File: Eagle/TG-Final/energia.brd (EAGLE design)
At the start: 172.7 x 172.7 mm, 55 parts, among them IC1 7812T, IC2 7805, IC3 AZ1117, IC4 7806T, Q1 TIP2955, T1 2N3904

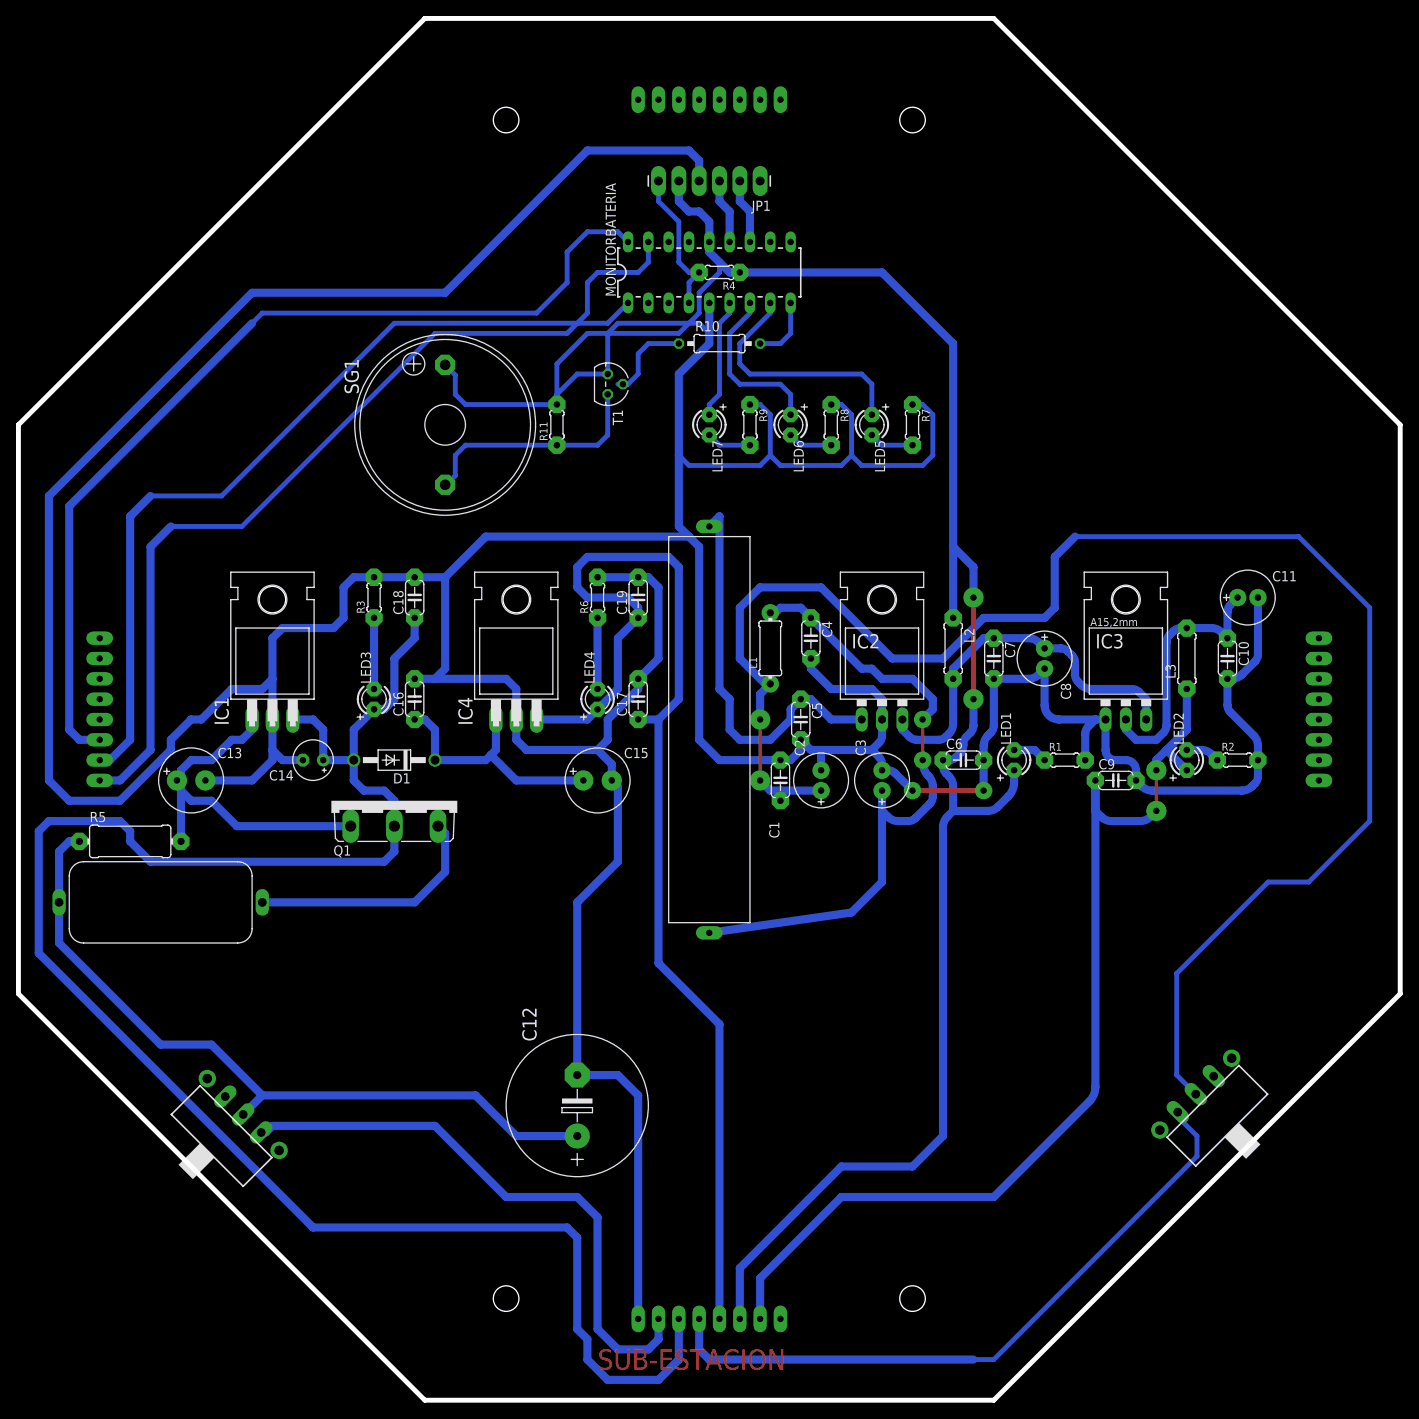
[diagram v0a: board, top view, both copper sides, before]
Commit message: Placa Sub-Estación. Lista
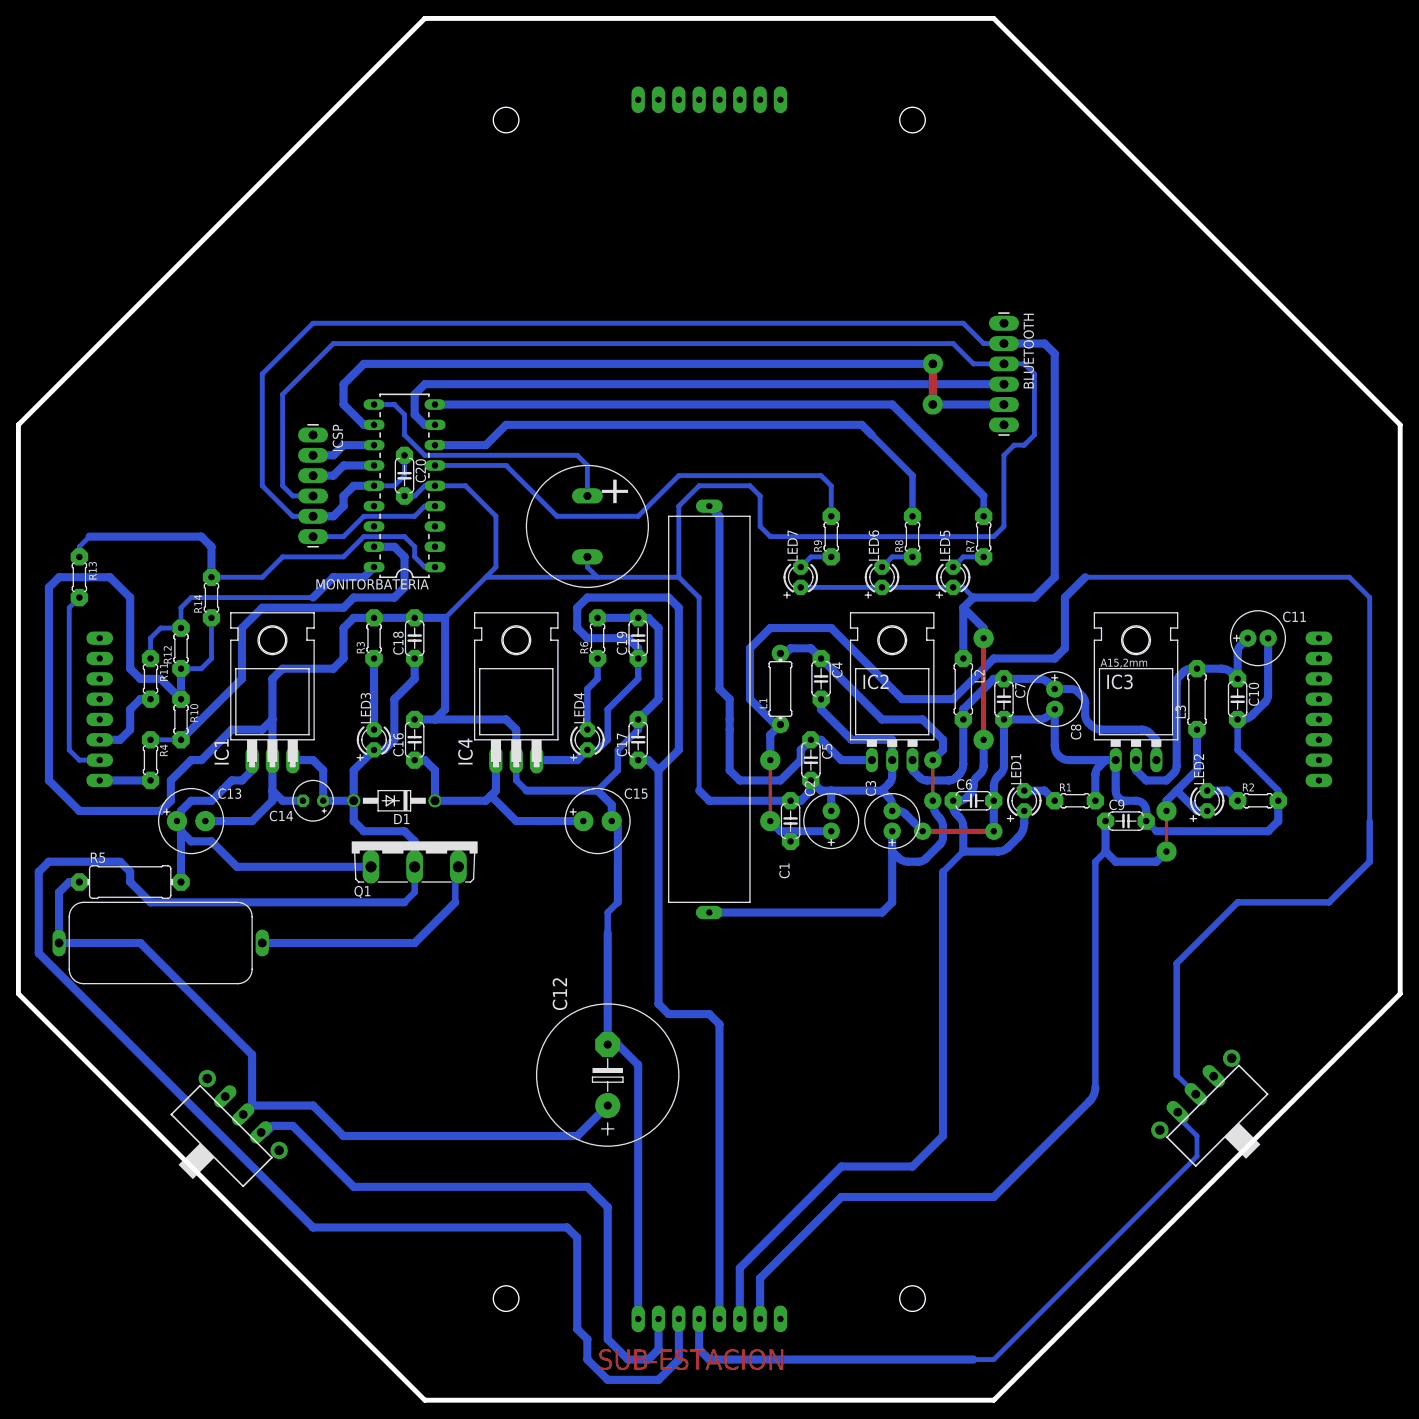
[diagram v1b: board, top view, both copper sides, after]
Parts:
- removed JP1: (no value), SparkFun:1X06_LONGPADS
- removed SG1: EB2209A, buzzer:EB2209A
- removed T1: 2N3904, transistor:TO92
- added BLUETOOTH, ICSP: (no value), SparkFun:1X06_LONGPADS
- added C20: 0.1uf, rcl:C050-024X044
- added R12, R14: 15K, rcl:0204/5
- added R13: 20K, rcl:0204/5
- added U$10: BUZZER, aasanchez:BUZZER
- LED5, LED6, LED7: value (none) -> RED
- R10: value 4K7 -> 15K; device rcl:0207/10 -> rcl:0204/5
- R11: value 4K7 -> 20K
- R4: value 1k -> 20K
- moved R4 93.7 mm to (-34.3, 80.0), turned to 270 degrees
- moved R10 82.1 mm to (-30.5, 85.1), turned to 270 degrees
- moved R11 59.9 mm to (-34.3, 90.2), turned to 270 degrees
- moved MONITORBATERIA 46.5 mm to (-2.54, 114.3), turned to 90 degrees
- moved LED6 22.2 mm to (57.1, 102.9), turned to 90 degrees
- moved LED7 22.2 mm to (47.0, 102.9), turned to 90 degrees
- moved LED5 21.6 mm to (66.0, 102.9), turned to 90 degrees
- moved R8 17.3 mm to (61.0, 108.0), turned to 90 degrees
- moved R9 17.3 mm to (50.8, 108.0), turned to 90 degrees
- moved R7 16.6 mm to (69.8, 108.0), turned to 90 degrees
- moved Q1 5.68 mm to (-1.27, 69.8)
- moved LED2 5.68 mm to (97.8, 74.9)
- moved R2 5.68 mm to (104.1, 74.9)
- moved C12 5.39 mm to (22.9, 40.6)
- moved IC3 5.24 mm to (88.9, 83.8)
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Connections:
- removed net N$23: MONITORBATERIA.9, R10.2
- removed net N$25: R11.1, SG1.-, T1.1
- new net AN0: MONITORBATERIA.17, R10.2, R4.1
- new net AN1: MONITORBATERIA.18, R11.1, R12.2
- new net AN2: MONITORBATERIA.1, R13.1, R14.2
- new net RX: BLUETOOTH.4, MONITORBATERIA.8
- new net TX: BLUETOOTH.5, MONITORBATERIA.11
- net N$15: now also R7.1; no longer R7.2
- net N$16: now also LED7.K, R9.1; no longer LED6.K, R8.2
- net N$19: now also LED6.K, R8.1; no longer LED7.K, R9.2
- net N$2: now also ICSP.6; no longer JP1.6, R4.2
- net N$20: now also R9.2; no longer LED7.A
- net N$21: now also R8.2; no longer LED6.A
- net N$22: now also MONITORBATERIA.9, R7.2; no longer LED5.A, MONITORBATERIA.8
- net N$24: now also MONITORBATERIA.10, U$10.+; no longer R10.1, T1.2
- net N$5: now also ICSP.3; no longer JP1.3
- net N$6: now also ICSP.2; no longer JP1.2
- net SENSE1: now also R4.2; no longer MONITORBATERIA.17
- net SENSE2: now also R11.2; no longer MONITORBATERIA.18
- net SENSE3: now also R13.2; no longer MONITORBATERIA.1
- net VDD: now also BLUETOOTH.2, C20.1, ICSP.5, LED5.A, LED6.A, LED7.A; no longer JP1.5, R11.2, R4.1, SG1.+
- net VSS: now also BLUETOOTH.3, C20.2, ICSP.4, R10.1, R12.1, R14.1, U$10.-; no longer JP1.4, R7.1, R8.1, R9.1, T1.3
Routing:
- net SENSE2: track 119.1 -> 9.94 mm
- net SENSE1: track 115.1 -> 6.35 mm
- net TX: track 0.00 -> 96.1 mm, vias 0 -> 2
- net SENSE3: track 106.1 -> 23.9 mm
- net RX: track 0.00 -> 79.8 mm
- net VDD: track 266.7 -> 331.4 mm
- net AN2: track 0.00 -> 55.0 mm
- net AN0: track 0.00 -> 51.5 mm
- net N$21: track 21.2 -> 68.5 mm
- net N$22: track 30.6 -> 75.9 mm
- net N$20: track 15.0 -> 58.6 mm
- net AN1: track 0.00 -> 35.7 mm
- net N$25: track 29.5 -> 0.00 mm
- net VSS: track 707.5 -> 734.9 mm
- net N$24: track 11.2 -> 35.1 mm
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
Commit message: Placa de Control Motores y Comunicación
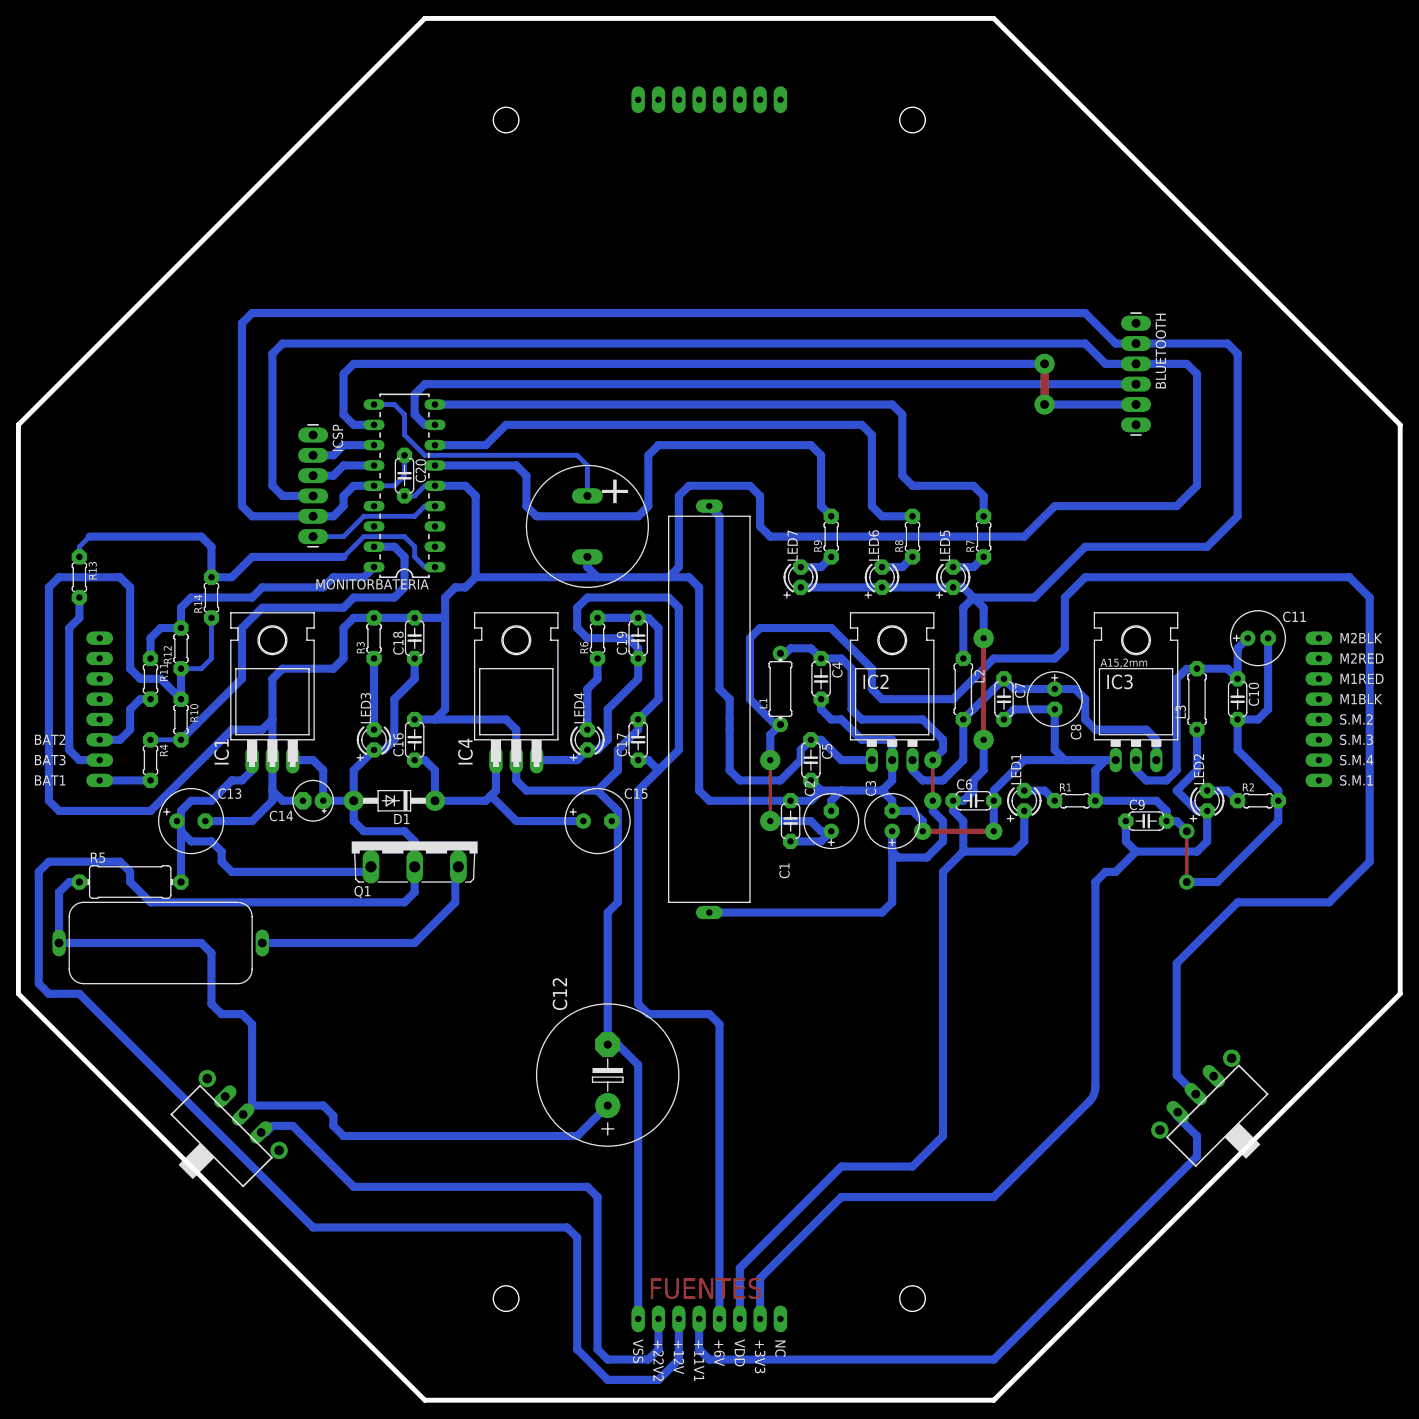
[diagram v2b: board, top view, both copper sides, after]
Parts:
- moved BLUETOOTH 16.5 mm to (88.9, 134.6)
- moved C9 2.54 mm to (90.2, 72.4)
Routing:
- net VSS: track 734.9 -> 794.8 mm, vias 2 -> 4
- net VDD: track 331.4 -> 386.3 mm
- net TX: track 96.1 -> 114.1 mm
- net RX: track 79.8 -> 96.3 mm
- net N$20: track 58.6 -> 69.2 mm
- net N$4: track 96.4 -> 103.1 mm
- net N$1: track 206.5 -> 213.1 mm
- net N$22: track 75.9 -> 80.3 mm
- net +6V: track 147.1 -> 150.7 mm
- net N$11: track 78.7 -> 82.0 mm
- net N$21: track 68.5 -> 70.7 mm
- net +12V: track 229.3 -> 230.9 mm
- net +22V: track 76.1 -> 77.6 mm
- net N$8: track 47.0 -> 48.2 mm
- net +3V3: track 121.5 -> 120.7 mm, vias 2 -> 0
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- added copper zone on layer 16, net VSS
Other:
- board text added: "FUENTES"
- board text removed: "SUB-ESTACION"
